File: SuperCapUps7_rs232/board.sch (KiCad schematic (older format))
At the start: 128 parts, among them J10 Conn_01x02, J11 Conn_01x02, J13 Conn_01x02, J14 Conn_01x02, J15 Conn_01x02, J20 connector_10pin_ISP_Console, J22 Conn_01x02, J3 Conn_02x03_Odd_Even, J79 Conn_01x04, J90 Conn_01x05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

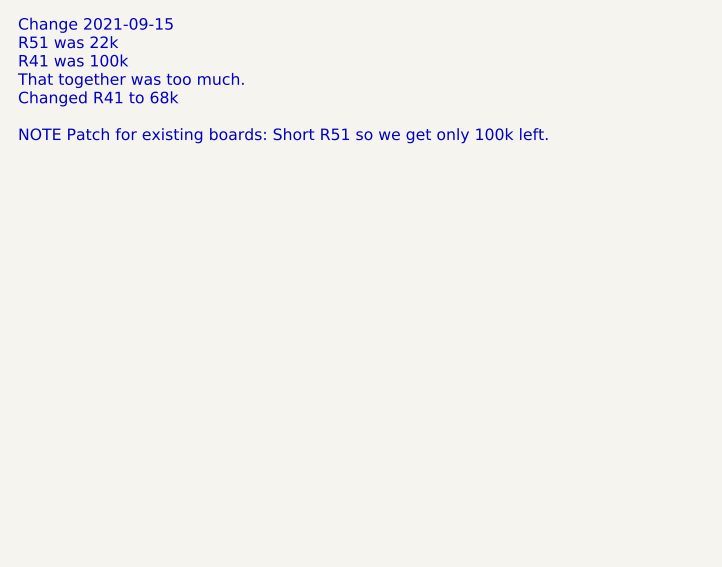
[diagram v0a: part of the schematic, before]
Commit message: This version was tested and something failed, see SuperCapUps7_rs232/bom.txt for details
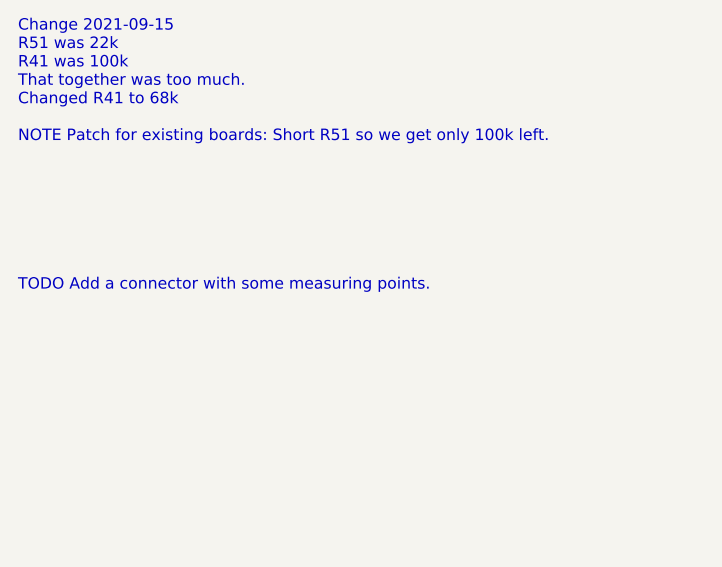
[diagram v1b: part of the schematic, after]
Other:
- note added: "TODO Add a connector with some measuring points."
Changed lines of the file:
@@
 EESchema Schematic File Version 4
-LIBS:board-cache
-EELAYER 26 0
+EELAYER 30 0
 EELAYER END
 $Descr A3 16535 11693
@@
 Text Notes -2850 6450 0    50   ~ 0
 Change 2021-09-15\nR51 was 22k\nR41 was 100k\nThat together was too much.\nChanged R41 to 68k\n\nNOTE Patch for existing boards: Short R51 so we get only 100k left.\n
+Text Notes -2850 7100 0    50   ~ 0
+TODO Add a connector with some measuring points.
 $EndSCHEMATC
